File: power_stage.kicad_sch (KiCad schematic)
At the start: 5 parts, among them IC3 2EDF7275F, J1 Input, J2 Output

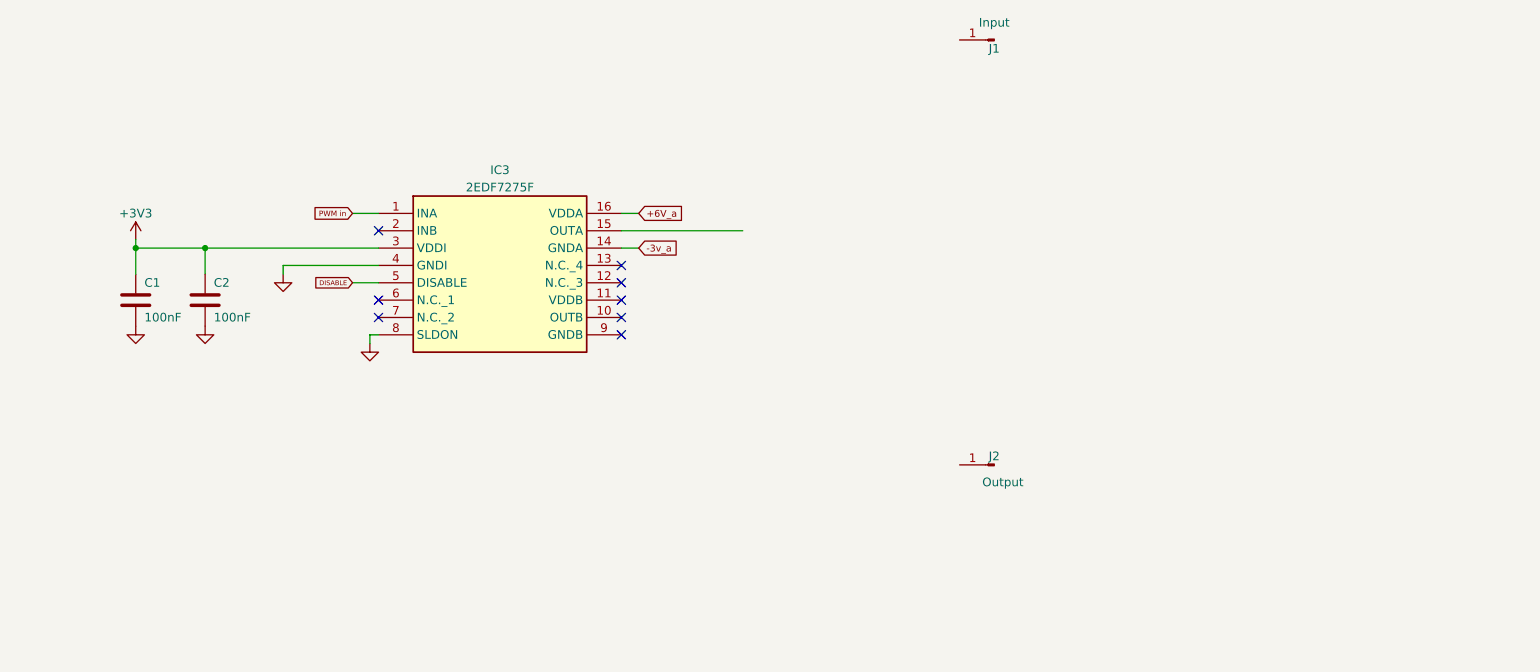
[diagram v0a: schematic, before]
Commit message: face to face switches design
with no MOVs and all other present
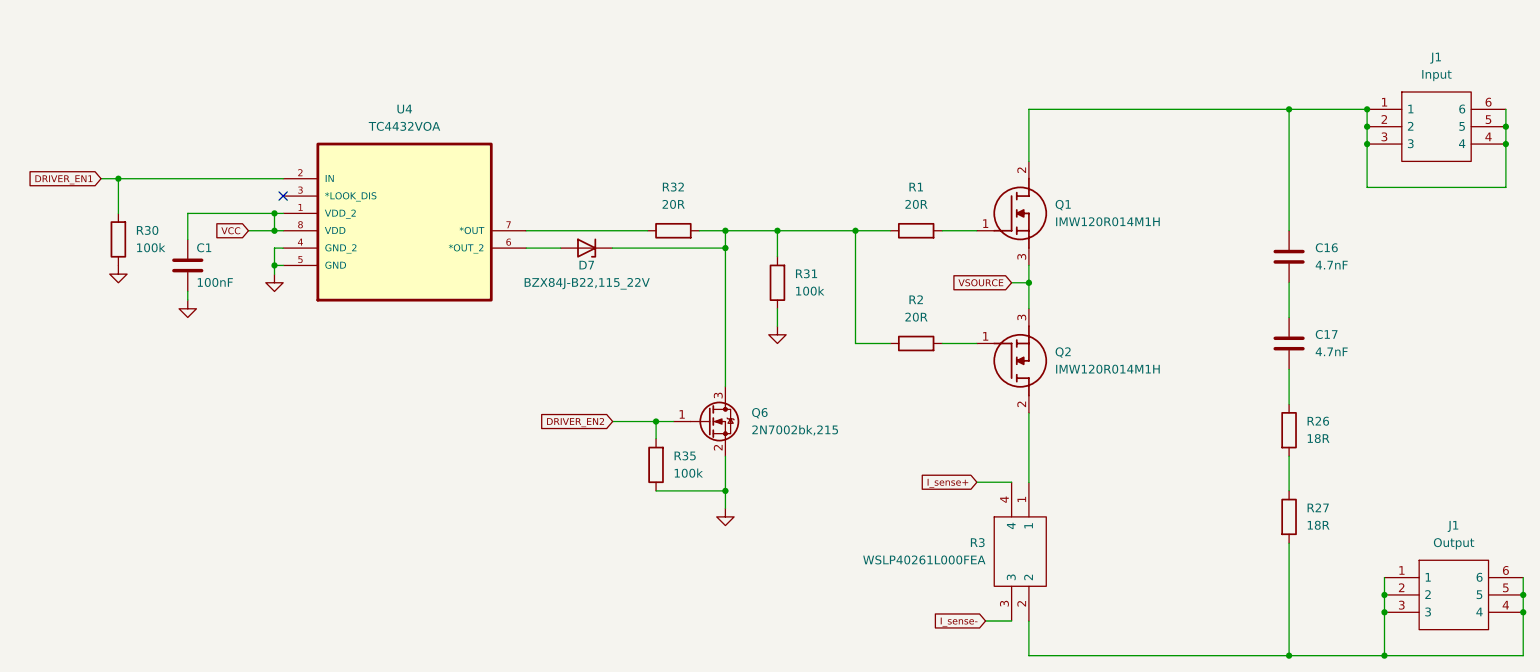
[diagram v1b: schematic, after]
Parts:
- removed C2: 100nF, symbol Device:C
- removed IC3: 2EDF7275F, KiCad:SOIC127P600X175-16N, symbol 2EDF7275F:2EDF7275F
- removed J1: Input, symbol Connector:Conn_01x01_Pin
- removed J2: Output, symbol Connector:Conn_01x01_Pin
- added C16, C17: 4.7nF, Capacitor_SMD:C_1812_4532Metric, symbol Device:C
- added D7: BZX84J-B22,115_22V, Package_TO_SOT_SMD:SOT-23, symbol Device:D_Zener
- added J1: Output, 7461057:7461057, symbol 7461057:7461057
- added J1: Input, 7461057:7461057, symbol 7461057:7461057
- added Q1, Q2: IMW120R014M1H, IMW120R014M1H:IMW120R014M1H, symbol IMW120R014M1H:IMW120R014M1H
- added Q6: 2N7002bk,215, Package_TO_SOT_SMD:SOT-23, symbol Transistor_FET:2N7002
- added R1, R2, R32: 20R, Resistor_SMD:R_0805_2012Metric, symbol Device:R
- added R26, R27: 18R, Resistor_SMD:R_2512_6332Metric, symbol Device:R
- added R3: WSLP40261L000FEA, WSLP40261L000FEA:WSLP40261L000FEA, symbol WSLP40261L000FEA:WSLP40261L000FEA
- added R30, R31, R35: 100k, Resistor_SMD:R_0805_2012Metric, symbol Device:R
- added U4: TC4432VOA, TC4432VOA:SOIC127P600X175-8N, symbol TC4432VOA:TC4432VOA
- C1: footprint (none) -> Capacitor_SMD:C_0805_2012Metric
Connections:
- net GND: now also Q6.2 (S), R30.1, R31.1, R35.1, U4.4 (GND_2), U4.5 (GND)
- net +3V3 renamed VCC
- net VCC: now also U4.1 (VDD_2), U4.8 (VDD)
- new net: C17.2, R26.1
- new net: R26.2, R27.1
- new net: D7.1 (K), Q6.3 (D), R1.1, R2.1, R31.2, R32.2
- new net: Q1.1 (G), R1.2
- new net: D7.2 (A), U4.6 (*OUT_2)
- new net: C16.2, C17.1
- new net: J1.1, J1.2, J1.3, J1.4, J1.5, J1.6, R27.2, R3.2
- new net: Q2.1 (G), R2.2
- new net: Q2.2 (D), R3.1
- new net: R32.1, U4.7 (*OUT)
- new net: C16.1, J1.1, J1.2, J1.3, J1.4, J1.5, J1.6, Q1.2 (D)
- new net DRIVER_EN1: R30.2, U4.2 (IN)
- new net DRIVER_EN2: Q6.1 (G), R35.2
- new net I_sense+: R3.4
- new net I_sense-: R3.3
- new net VSOURCE: Q1.3 (S), Q2.3 (S)
- no-connect marks 8 -> 1
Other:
- moved on the sheet: C1
